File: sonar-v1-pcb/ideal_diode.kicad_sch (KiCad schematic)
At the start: 4 parts, among them Q1 AO3415, U2 DZDH0401DW-7

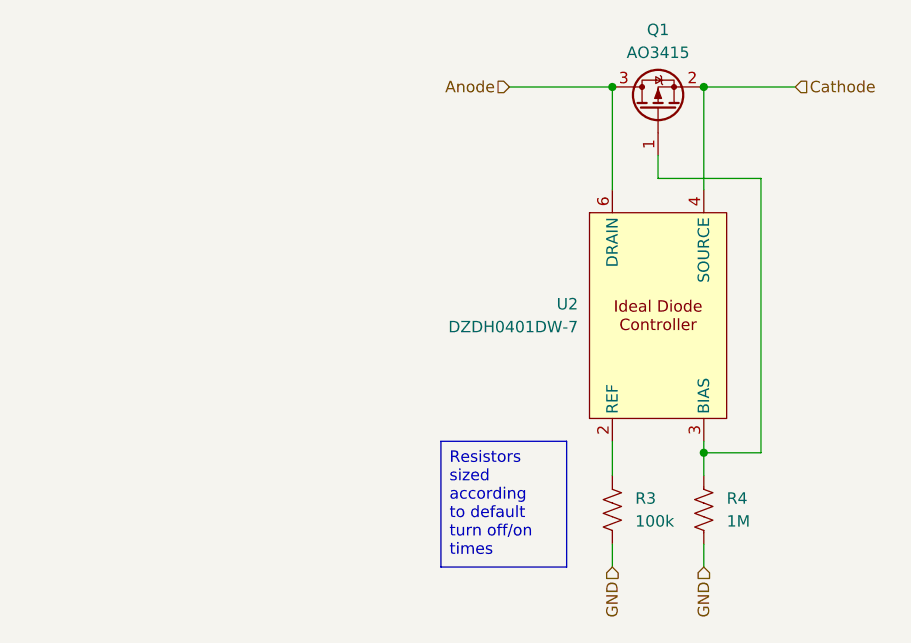
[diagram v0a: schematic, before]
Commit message: WIP hand-off: rx amp sim project, SPICE models, schematic updates
Adds rx_amp_sim KiCad project, SPICE models, Python setup-kicad.py
(replaces test_py.sh), CLAUDE.md, and a sweep of schematic edits across
the v1 board.

Co-Authored-By: Claude Opus 4.7 <noreply@anthropic.com>
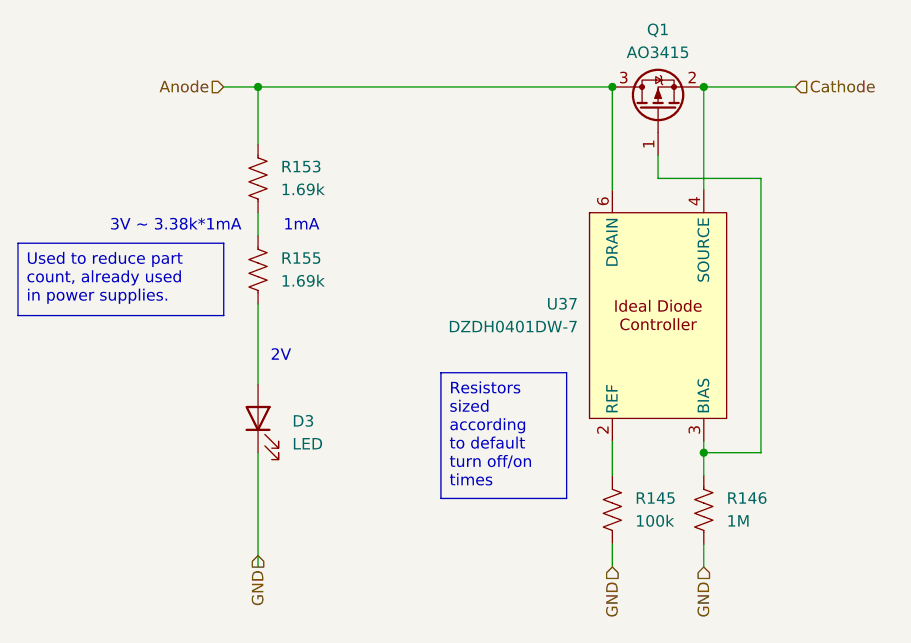
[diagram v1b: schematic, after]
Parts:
- added D3: LED, LED_SMD:LED_0603_1608Metric, symbol Device:LED
- added R153, R155: 1.69k, Sonar:R_0603_1608Metric, symbol sonar_lib:R_0603_1.69k
- R146: renamed from R4; footprint GS_Resistors:R_0603_1608Metric -> Sonar:R_0603_1608Metric
- renumbered R3 to R145, U2 to U37
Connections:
- net Anode: now also R153.1
- net GND: now also D3.1 (K)
- new net: R153.2, R155.1
- new net: D3.2 (A), R155.2
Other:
- note added: "1mA"
- note added: "2V"
- note added: "3V ~ 3.38k*1mA"
